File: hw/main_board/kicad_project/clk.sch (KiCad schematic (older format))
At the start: 4 parts

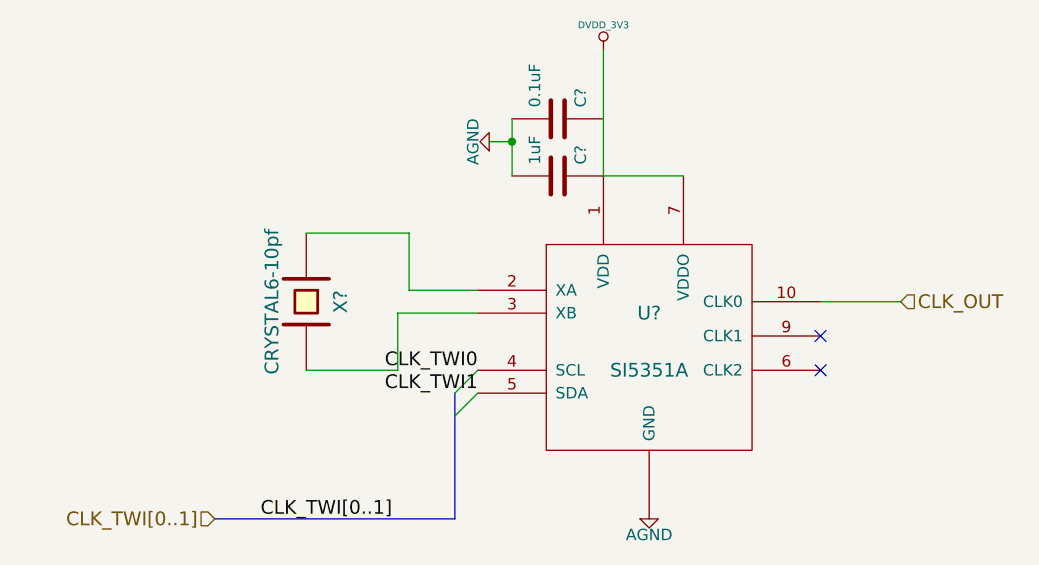
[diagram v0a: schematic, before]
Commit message: started mainboard pcb layout, fixing small things in schematic, TODO: schematic connector symbols and pads
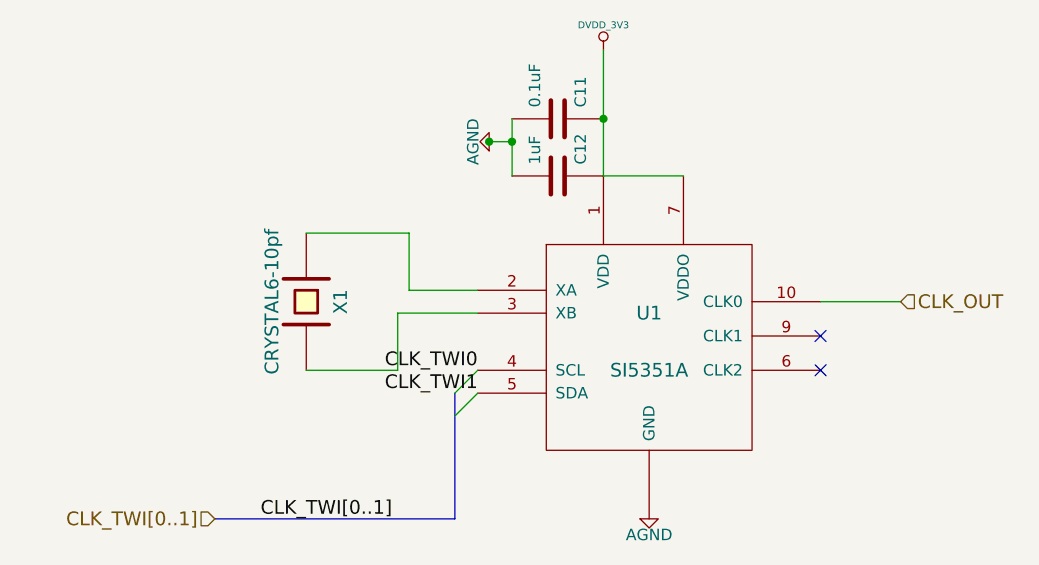
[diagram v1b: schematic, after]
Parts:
- C11, C12: renamed from C?; footprint (none) -> 0603
- U1: renamed from U?; footprint (none) -> QSOP_16
- X1: renamed from X?; footprint (none) -> ECX_53B
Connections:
- net DVDD_3V3: now also C11.1
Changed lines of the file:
@@
 $Descr A4 11693 8268
 encoding utf-8
-Sheet 6 7
-Title ""
-Date ""
-Rev ""
+Sheet 5 7
+Title "Clock"
+Date "01 Feb 2014"
+Rev "A"
 Comp ""
-Comment1 ""
+Comment1 "Copyright 2014 Andrey Shmakov"
 Comment2 ""
 Comment3 ""
@@
 $EndDescr
 $Comp
-L DVDD_3V3 #PWR?
+L DVDD_3V3 #PWR027
 U 1 1 5316C694
 P 5950 3300
-F 0 "#PWR?" H 5950 3400 30  0001 C CNN
+F 0 "#PWR027" H 5950 3400 30  0001 C CNN
 F 1 "DVDD_3V3" H 5950 3410 30  0000 C CNN
 F 2 "" H 5950 3300 60  0001 C CNN
@@
 $EndComp
 $Comp
-L C C?
+L C C12
 U 1 1 5316C69A
 P 5750 3850
-F 0 "C?" H 5800 3950 50  0000 L CNN
+F 0 "C12" H 5800 3950 50  0000 L CNN
 F 1 "1uF" H 5800 3750 50  0000 L CNN
-F 2 "" H 5750 3850 60  0001 C CNN
+F 2 "0603" H 5750 3850 60  0001 C CNN
 F 3 "" H 5750 3850 60  0001 C CNN
 	1    5750 3850
@@
 $EndComp
 $Comp
-L C C?
+L C C11
 U 1 1 5316C6A0
 P 5750 3600
-F 0 "C?" H 5800 3700 50  0000 L CNN
+F 0 "C11" H 5800 3700 50  0000 L CNN
 F 1 "0.1uF" H 5800 3500 50  0000 L CNN
-F 2 "" H 5750 3600 60  0001 C CNN
+F 2 "0603" H 5750 3600 60  0001 C CNN
 F 3 "" H 5750 3600 60  0001 C CNN
 	1    5750 3600
@@
 $EndComp
 $Comp
-L AGND #PWR?
+L AGND #PWR028
 U 1 1 5316C6A6
 P 5450 3700
-F 0 "#PWR?" H 5450 3700 40  0001 C CNN
+F 0 "#PWR028" H 5450 3700 40  0001 C CNN
 F 1 "AGND" H 5450 3630 50  0000 C CNN
 F 2 "" H 5450 3700 60  0001 C CNN
@@
 	5300 4800 5400 4700
 $Comp
-L AGND #PWR?
+L AGND #PWR029
 U 1 1 5316C6B0
 P 6150 5350
-F 0 "#PWR?" H 6150 5350 40  0001 C CNN
+F 0 "#PWR029" H 6150 5350 40  0001 C CNN
 F 1 "AGND" H 6150 5280 50  0000 C CNN
 F 2 "" H 6150 5350 60  0001 C CNN
@@
 $EndComp
 $Comp
-L CRYSTAL X?
+L CRYSTAL X1
 U 1 1 5316C6B6
 P 4650 4400
-F 0 "X?" H 4650 4550 60  0000 C CNN
+F 0 "X1" H 4650 4550 60  0000 C CNN
 F 1 "CRYSTAL6-10pf" H 4650 4250 60  0000 C CNN
-F 2 "" H 4650 4400 60  0001 C CNN
+F 2 "ECX_53B" H 4650 4400 60  0001 C CNN
 F 3 "" H 4650 4400 60  0001 C CNN
 	1    4650 4400
@@
 NoConn ~ 6900 4700
 $Comp
-L SI5351A U?
+L SI5351A U1
 U 1 1 5316C6BE
 P 6150 4600
-F 0 "U?" H 6150 4750 60  0000 C CNN
+F 0 "U1" H 6150 4750 60  0000 C CNN
 F 1 "SI5351A" H 6150 4500 60  0000 C CNN
-F 2 "" H 6150 4600 60  0001 C CNN
+F 2 "QSOP_16" H 6150 4600 60  0001 C CNN
 F 3 "" H 6150 4600 60  0001 C CNN
 	1    6150 4600
@@
 Text Label 4450 5350 0    60   ~ 0
 CLK_TWI[0..1]
+Connection ~ 5950 3600
+Connection ~ 5450 3700
 $EndSCHEMATC

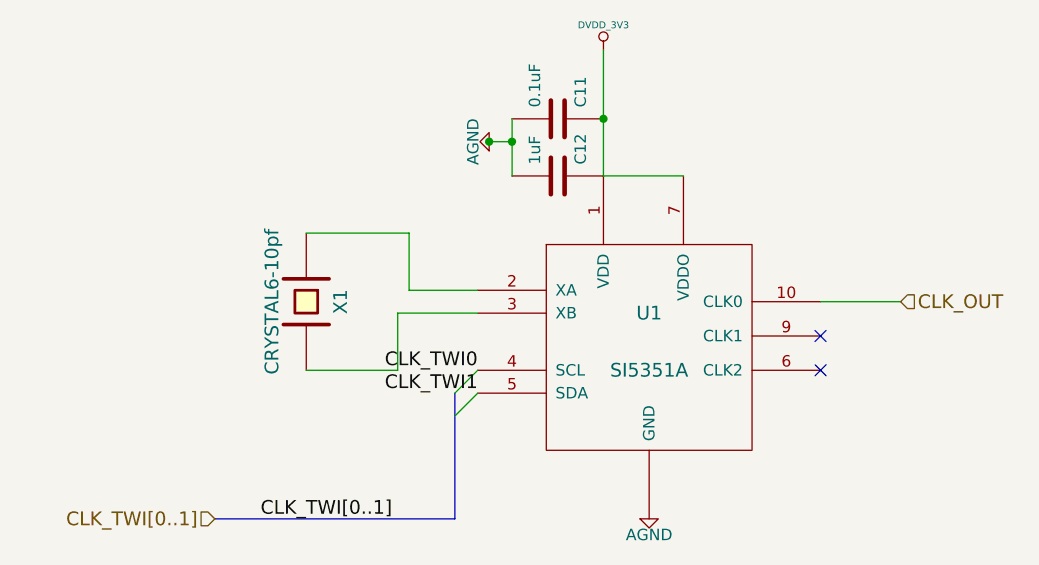
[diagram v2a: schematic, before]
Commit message: finished component layout on mainboard, need to route power planes and the digital control signal lines
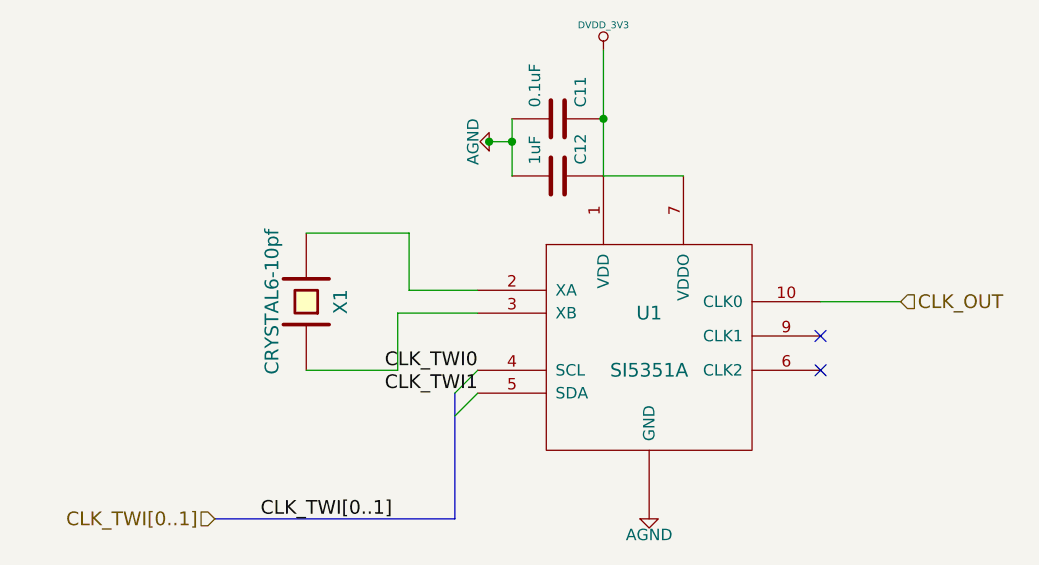
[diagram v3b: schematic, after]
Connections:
- net at X1.1: now also U1.3 (XB); no longer U1.2 (XA)
- net at X1.2: now also U1.2 (XA); no longer U1.3 (XB)
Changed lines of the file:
@@
 EESchema Schematic File Version 2
 LIBS:ddslib
+LIBS:demuxcomplib
 LIBS:tDCS_driver-cache
 EELAYER 24 0
@@
 $EndDescr
 $Comp
-L DVDD_3V3 #PWR033
+L DVDD_3V3 #PWR032
 U 1 1 5316C694
 P 5950 3300
-F 0 "#PWR033" H 5950 3400 30  0001 C CNN
+F 0 "#PWR032" H 5950 3400 30  0001 C CNN
 F 1 "DVDD_3V3" H 5950 3410 30  0000 C CNN
 F 2 "" H 5950 3300 60  0001 C CNN
@@
 $EndComp
 $Comp
-L AGND #PWR034
+L AGND #PWR033
 U 1 1 5316C6A6
 P 5450 3700
-F 0 "#PWR034" H 5450 3700 40  0001 C CNN
+F 0 "#PWR033" H 5450 3700 40  0001 C CNN
 F 1 "AGND" H 5450 3630 50  0000 C CNN
 F 2 "" H 5450 3700 60  0001 C CNN
@@
 	5300 4800 5400 4700
 $Comp
-L AGND #PWR035
+L AGND #PWR034
 U 1 1 5316C6B0
 P 6150 5350
-F 0 "#PWR035" H 6150 5350 40  0001 C CNN
+F 0 "#PWR034" H 6150 5350 40  0001 C CNN
 F 1 "AGND" H 6150 5280 50  0000 C CNN
 F 2 "" H 6150 5350 60  0001 C CNN
@@
 F 3 "" H 4650 4400 60  0001 C CNN
 	1    4650 4400
-	0    1    1    0
+	0    1    -1   0
 $EndComp
-NoConn ~ 6900 4550
-NoConn ~ 6900 4700
 $Comp
 L SI5351A U1
@@
 Connection ~ 5950 3600
 Connection ~ 5450 3700
+NoConn ~ 6900 4550
+NoConn ~ 6900 4700
 $EndSCHEMATC
